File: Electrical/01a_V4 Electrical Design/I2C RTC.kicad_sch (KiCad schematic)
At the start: 54 parts, among them J17 B4B-PH-SM4-TB(LF)(SN), J20 B4B-PH-SM4-TB(LF)(SN), U10 TCA9534DWR, U3 TCA9534DWR, U6 NCT175DMR2G, U7 TCA9534DWR, U8 NCT175DMR2G, U9 VEML7700-TR

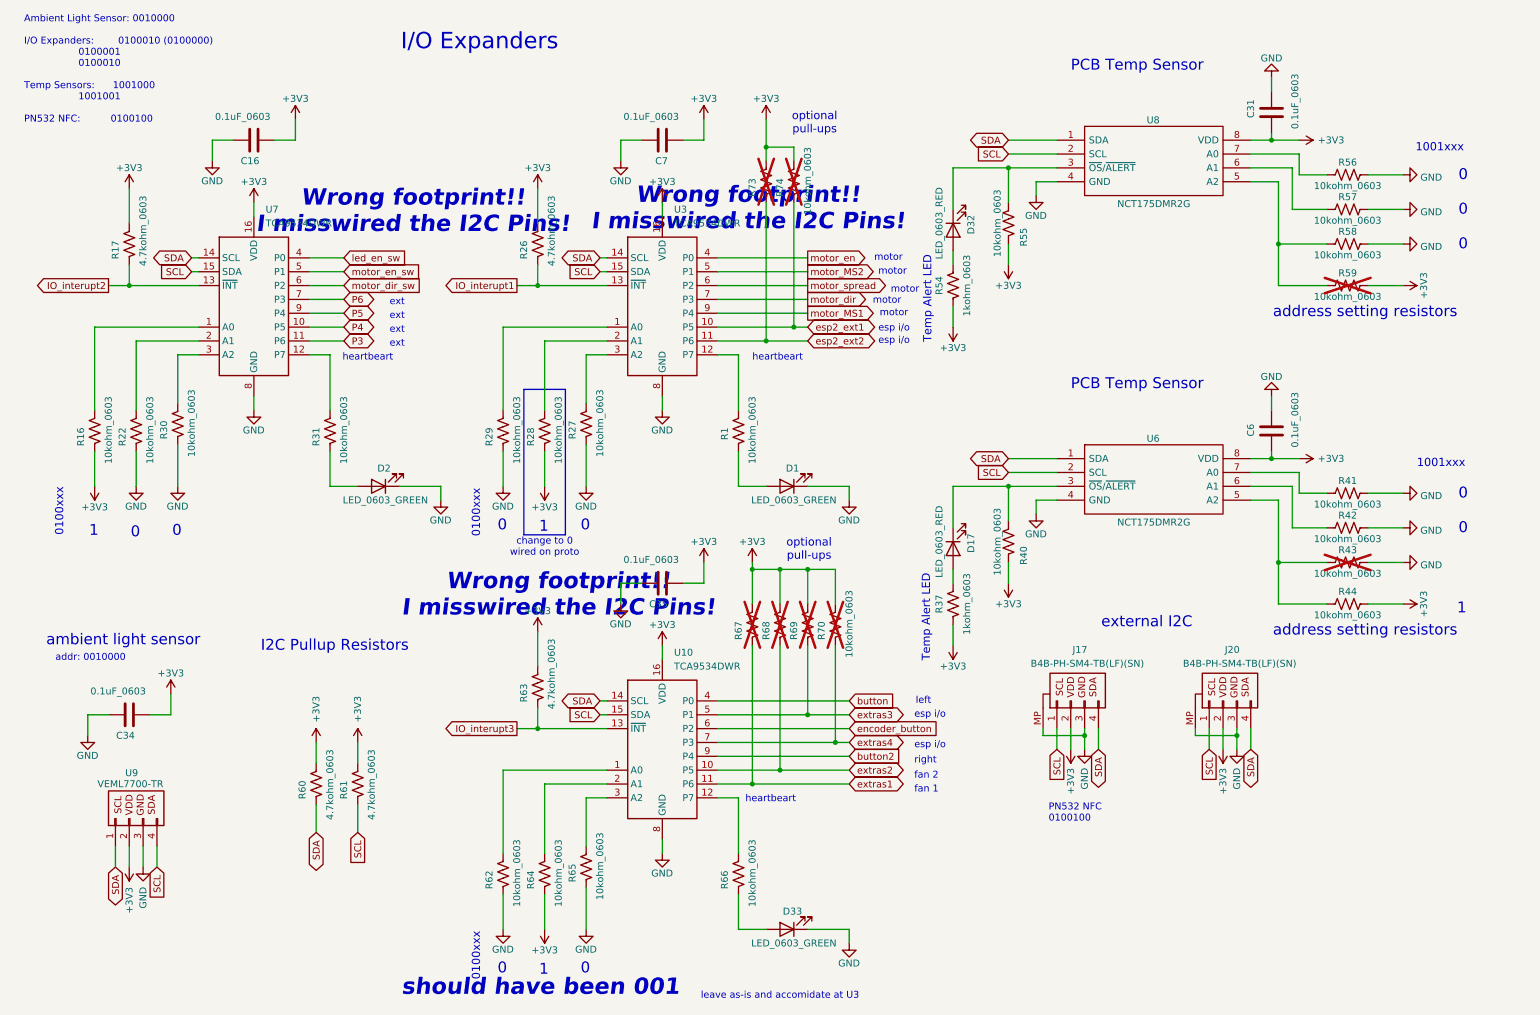
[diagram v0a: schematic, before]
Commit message: main schematic tweaks. Started the 'Saber' PCB which is the new end effector for the strobe light. Schematic nearly finished. Need to create footprint for LEDs and layout the board to be CNC milled.
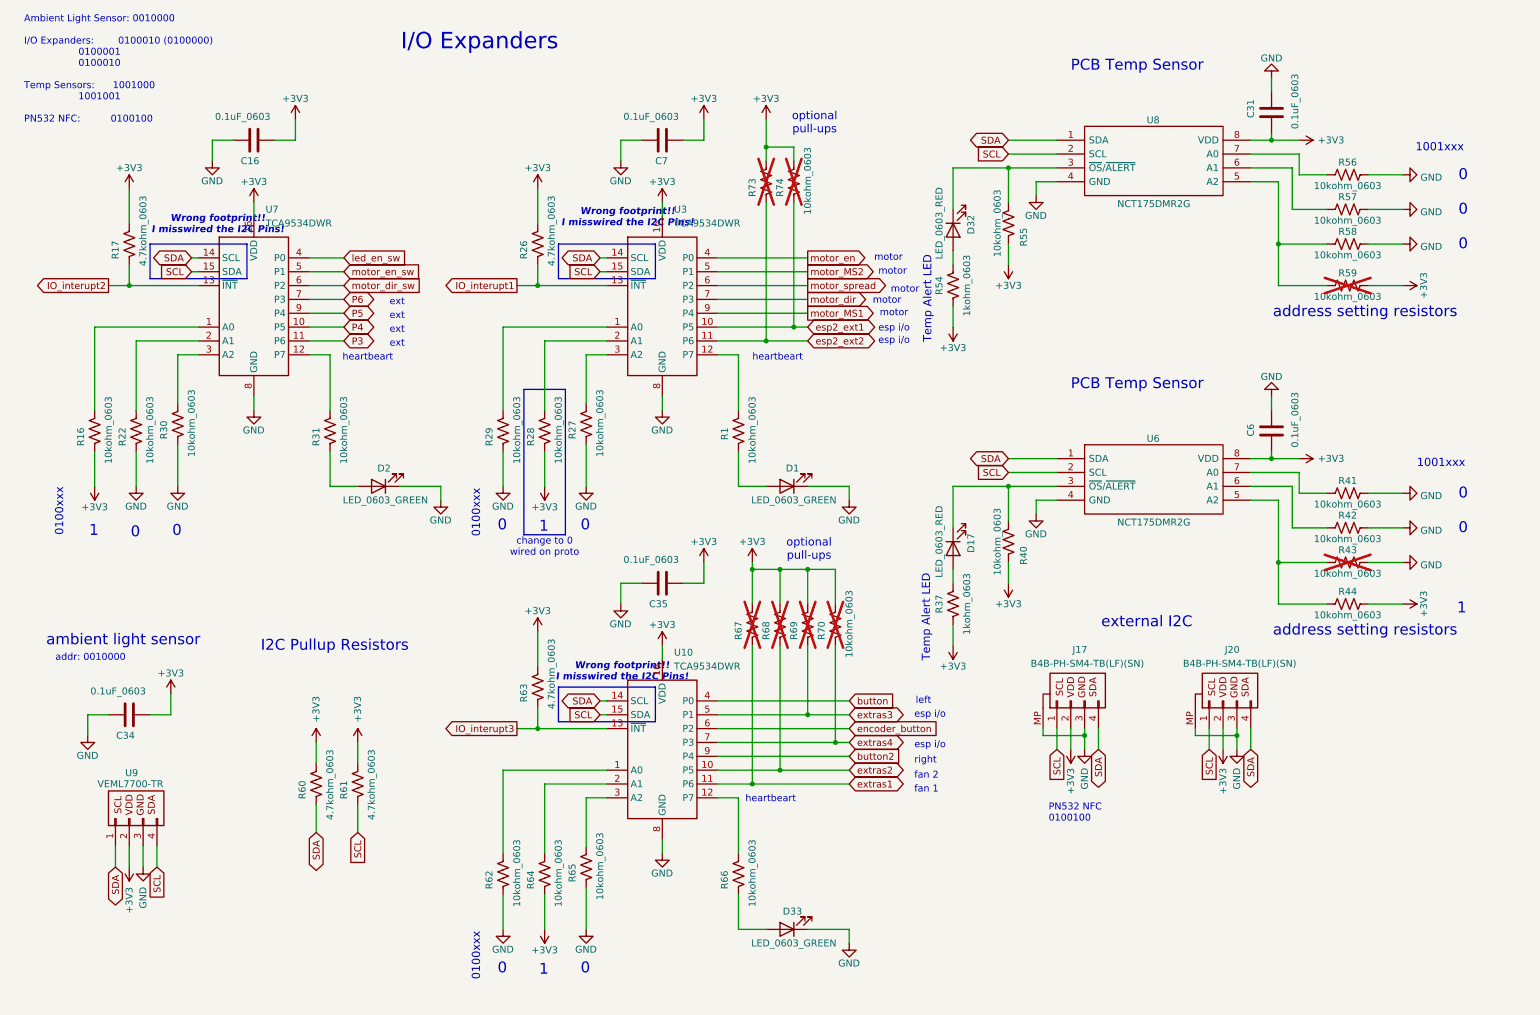
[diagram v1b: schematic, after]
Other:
- note removed: "leave as-is and accomidate at U3"
- note removed: "should have been 001"
- company: (none) -> Kadin Whiting
- title: (none) -> I2C Devices
